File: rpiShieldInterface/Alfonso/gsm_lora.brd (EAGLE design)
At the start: 65.2 x 56 mm, 57 parts

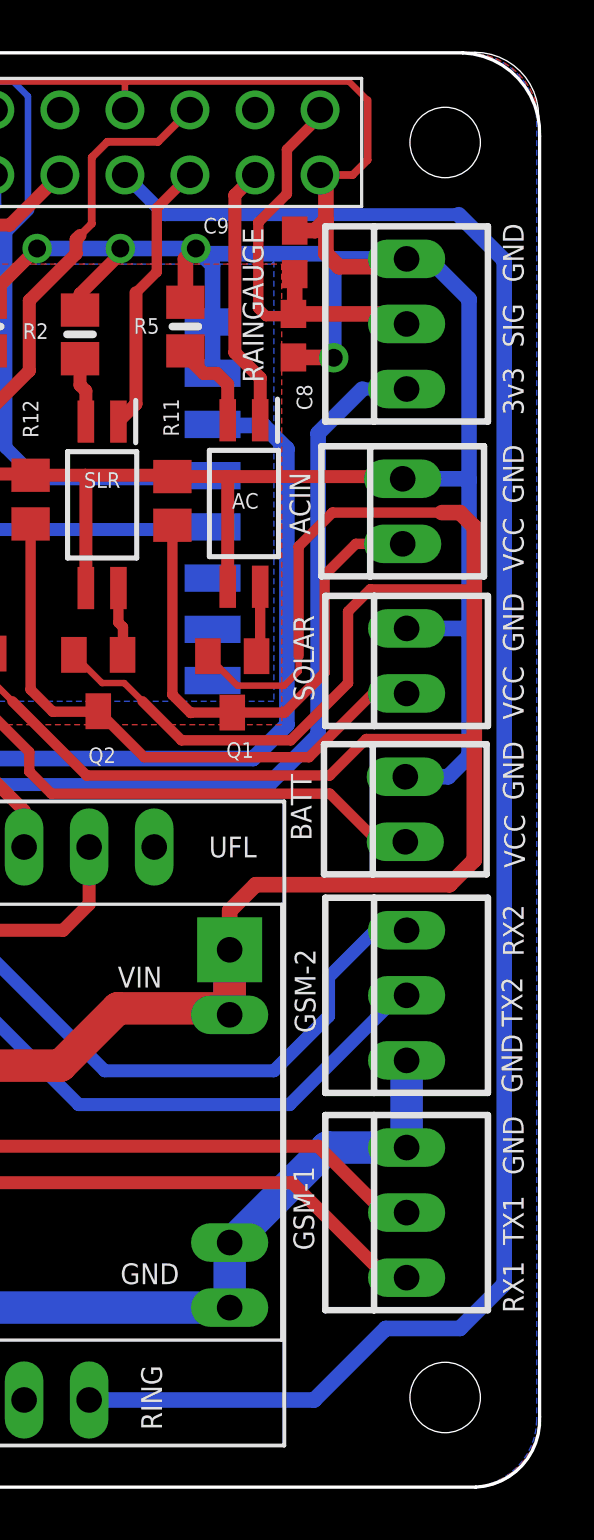
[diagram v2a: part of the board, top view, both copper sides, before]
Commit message: finalize gerber files repair outline of board
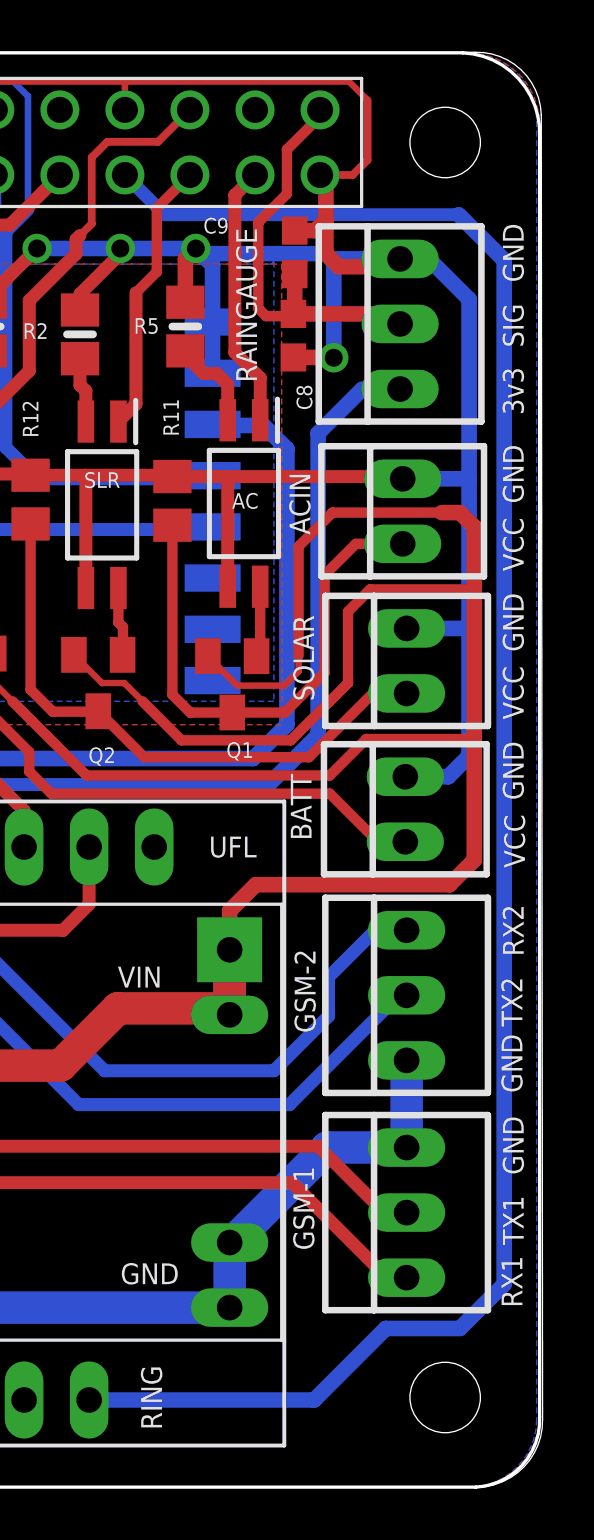
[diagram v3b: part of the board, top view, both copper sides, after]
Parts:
- moved RAINGAUGE 0.25 mm to (60.3, 45.9)
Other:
- board size 65.2 x 56 mm -> 65.4 x 56 mm
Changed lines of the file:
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@@
 <plain>
 <wire x1="3.2004" y1="0.508" x2="63.3224" y2="0.508" width="0" layer="20"/>
-<wire x1="63.3224" y1="0.508" x2="65.71" y2="3.0988" width="0" layer="20" curve="90"/>
-<wire x1="65.71" y1="3.0988" x2="65.71" y2="54.0412" width="0" layer="20"/>
-<wire x1="65.71" y1="54.0412" x2="63.2208" y2="56.5304" width="0" layer="20" curve="90"/>
+<wire x1="63.3224" y1="0.508" x2="65.8624" y2="3.1496" width="0" layer="20" curve="90"/>
+<wire x1="65.8624" y1="3.1496" x2="65.8116" y2="54.092" width="0" layer="20"/>
+<wire x1="65.8116" y1="54.092" x2="63.2208" y2="56.5304" width="0" layer="20" curve="90"/>
 <wire x1="63.2208" y1="56.5304" x2="3.0988" y2="56.5304" width="0" layer="20"/>
 <wire x1="3.0988" y1="56.5304" x2="0.508" y2="53.9904" width="0" layer="20" curve="90"/>
@@
 <text x="65.1764" y="24.6888" size="0.8128" layer="25" ratio="10" rot="R90">VCC</text>
 <text x="65.1256" y="9.9568" size="0.8128" layer="25" ratio="10" rot="R90">TX1</text>
-<text x="65.1256" y="7.3152" size="0.8128" layer="25" ratio="10" rot="R90">RX1</text>
+<text x="65.0748" y="7.5184" size="0.8128" layer="25" ratio="10" rot="R90">RX1</text>
 <text x="65.0748" y="18.4912" size="0.8128" layer="25" ratio="10" rot="R90">TX2</text>
 <text x="65.1256" y="21.2344" size="0.8128" layer="25" ratio="10" rot="R90">RX2</text>
@@
 <attribute name="VALUE" x="65.6336" y="15.9004" size="1.016" layer="27" ratio="10" rot="R90"/>
 </element>
-<element name="RAINGAUGE" library="con-molex" library_urn="urn:adsk.eagle:library:165" package="22-23-2031" value="Rain Gauge" x="60.5536" y="45.9232" rot="R90">
-<attribute name="MF" value="MOLEX" x="60.5536" y="45.9232" size="1.778" layer="27" rot="R90" display="off"/>
-<attribute name="MPN" value="22-23-2031" x="60.5536" y="45.9232" size="1.778" layer="27" rot="R90" display="off"/>
-<attribute name="NAME" x="54.9656" y="43.6372" size="0.8128" layer="25" ratio="10" rot="R90"/>
-<attribute name="OC_FARNELL" value="1462950" x="60.5536" y="45.9232" size="1.778" layer="27" rot="R90" display="off"/>
-<attribute name="OC_NEWARK" value="30C0862" x="60.5536" y="45.9232" size="1.778" layer="27" rot="R90" display="off"/>
-<attribute name="VALUE" x="65.6336" y="42.1132" size="1.016" layer="27" ratio="10" rot="R90"/>
+<element name="RAINGAUGE" library="con-molex" library_urn="urn:adsk.eagle:library:165" package="22-23-2031" value="Rain Gauge" x="60.2996" y="45.9232" rot="R90">
+<attribute name="MF" value="MOLEX" x="60.2996" y="45.9232" size="1.778" layer="27" rot="R90" display="off"/>
+<attribute name="MPN" value="22-23-2031" x="60.2996" y="45.9232" size="1.778" layer="27" rot="R90" display="off"/>
+<attribute name="NAME" x="54.7116" y="43.6372" size="0.8128" layer="25" ratio="10" rot="R90"/>
+<attribute name="OC_FARNELL" value="1462950" x="60.2996" y="45.9232" size="1.778" layer="27" rot="R90" display="off"/>
+<attribute name="OC_NEWARK" value="30C0862" x="60.2996" y="45.9232" size="1.778" layer="27" rot="R90" display="off"/>
+<attribute name="VALUE" x="65.3796" y="42.1132" size="1.016" layer="27" ratio="10" rot="R90"/>
 </element>
 <element name="C8" library="rcl" library_urn="urn:adsk.eagle:library:334" package="C0603" package3d_urn="urn:adsk.eagle:package:23616@1/2" value="0.1nF" x="56.134" y="45.466" rot="R270">
@@
 <via x="7.0104" y="47.752" extent="1-16" drill="0.7" diameter="1.15"/>
 <wire x1="57.6072" y1="48.4632" x2="57.404" y2="48.6664" width="0.6096" layer="16"/>
-<wire x1="60.5536" y1="48.4632" x2="57.7088" y2="48.4632" width="0.6096" layer="16"/>
+<wire x1="60.2996" y1="48.4632" x2="57.7088" y2="48.4632" width="0.6096" layer="16"/>
 <wire x1="57.7088" y1="48.4632" x2="57.6072" y2="48.4632" width="0.6096" layer="16"/>
 <wire x1="57.404" y1="48.6664" x2="52.5272" y2="48.6664" width="0.6096" layer="16"/>
@@
 <wire x1="57.404" y1="49.9872" x2="57.404" y2="48.6664" width="0.6096" layer="1"/>
 <wire x1="57.404" y1="48.6664" x2="57.912" y2="48.1584" width="0.6096" layer="1"/>
-<wire x1="60.5536" y1="48.1584" x2="57.912" y2="48.1584" width="0.6096" layer="1"/>
+<wire x1="60.2996" y1="48.1584" x2="57.912" y2="48.1584" width="0.6096" layer="1"/>
 <wire x1="44.196" y1="46.9392" x2="44.196" y2="46.7716" width="0.508" layer="1"/>
 <wire x1="46.1264" y1="48.8696" x2="44.196" y2="46.9392" width="0.508" layer="1"/>
@@
 <wire x1="47.8028" y1="47.0916" x2="49.3776" y2="48.6664" width="0.508" layer="1"/>
 <wire x1="31.7754" y1="54.2798" x2="33.02" y2="53.0352" width="0.4064" layer="1"/>
-<wire x1="60.5536" y1="48.4632" x2="60.5536" y2="48.1584" width="0.4064" layer="1"/>
+<wire x1="60.2996" y1="48.4632" x2="60.2996" y2="48.1584" width="0.4064" layer="1"/>
 <wire x1="57.1754" y1="51.7398" x2="57.404" y2="51.5112" width="0.4064" layer="1"/>
 <wire x1="19.0754" y1="51.7398" x2="18.9992" y2="51.6636" width="0.4064" layer="16"/>
@@
 <wire x1="53.5686" y1="35.6628" x2="53.5686" y2="39.939" width="0.508" layer="1"/>
 <wire x1="53.5686" y1="39.939" x2="53.5432" y2="39.9644" width="0.508" layer="1"/>
-<wire x1="60.5536" y1="48.4632" x2="61.4172" y2="48.4632" width="0.6096" layer="16"/>
+<wire x1="61.4172" y1="48.4632" x2="60.2996" y2="48.4632" width="0.6096" layer="16"/>
 <wire x1="61.4172" y1="48.4632" x2="62.992" y2="46.8884" width="0.6096" layer="16"/>
 <wire x1="62.992" y1="46.8884" x2="62.992" y2="39.8272" width="0.6096" layer="16"/>
@@
 <wire x1="56.1848" y1="47.8672" x2="56.1848" y2="46.3668" width="0.6096" layer="1"/>
 <wire x1="56.1848" y1="46.3668" x2="56.134" y2="46.316" width="0.6096" layer="1"/>
-<wire x1="56.134" y1="46.316" x2="60.1608" y2="46.316" width="0.6096" layer="1"/>
-<wire x1="60.1608" y1="46.316" x2="60.5536" y2="45.9232" width="0.6096" layer="1"/>
+<wire x1="56.134" y1="46.316" x2="59.9068" y2="46.316" width="0.6096" layer="1"/>
+<wire x1="60.2996" y1="45.9232" x2="59.9068" y2="46.316" width="0.6096" layer="1"/>
 <wire x1="57.1754" y1="54.2798" x2="57.1754" y2="54.0258" width="0.4064" layer="1"/>
 <wire x1="57.1754" y1="54.0258" x2="55.88" y2="52.7304" width="0.4064" layer="1"/>
@@
 <wire x1="32.004" y1="37.3888" x2="32.004" y2="30.8864" width="0.508" layer="16"/>
 <wire x1="34.9504" y1="27.94" x2="32.004" y2="30.8864" width="0.508" layer="16"/>
-<wire x1="60.5536" y1="43.3832" x2="58.8264" y2="43.3832" width="0.508" layer="16"/>
+<wire x1="60.2996" y1="43.3832" x2="58.8264" y2="43.3832" width="0.508" layer="16"/>
 <wire x1="55.1688" y1="27.94" x2="34.9504" y2="27.94" width="0.508" layer="16"/>
 <wire x1="32.004" y1="37.3888" x2="31.1912" y2="38.2016" width="0.508" layer="16"/>
